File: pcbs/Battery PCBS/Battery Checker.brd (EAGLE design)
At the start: 49.5 x 49.5 mm, 26 parts, among them Q1 BSS138, Q2 BSS138

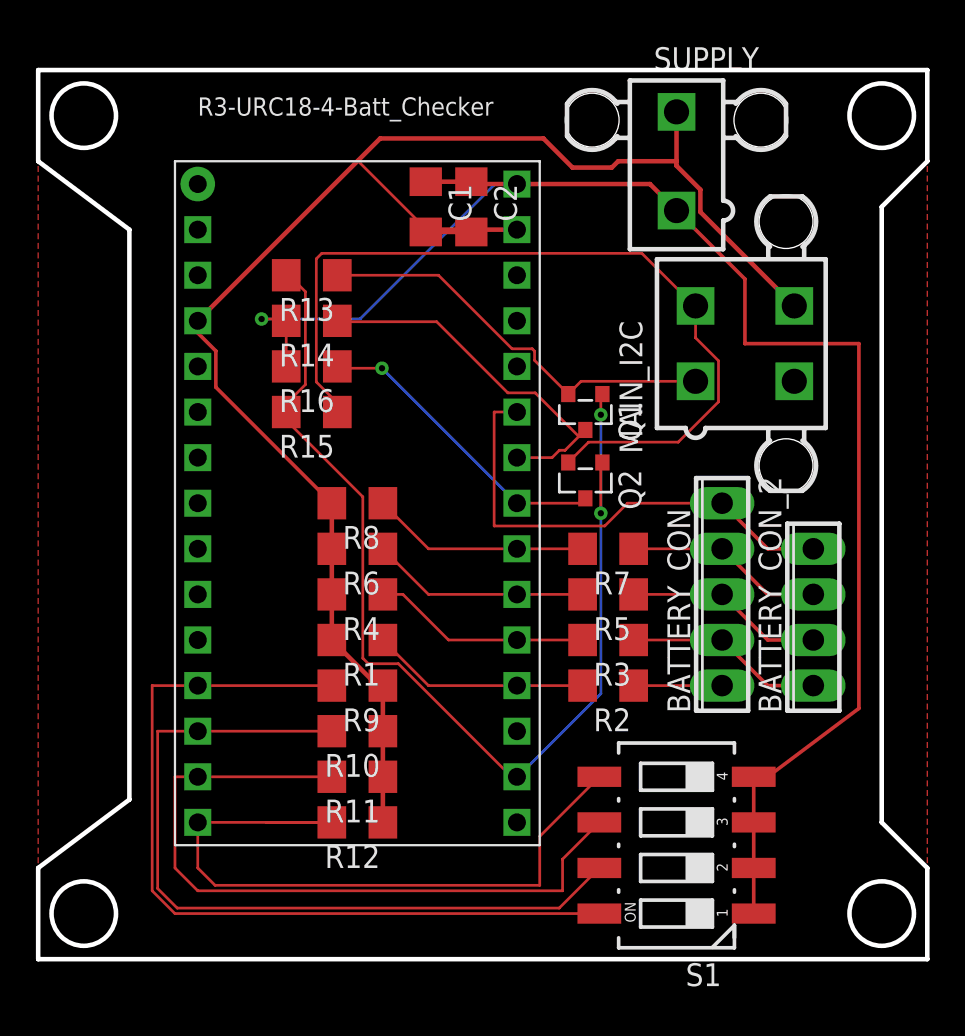
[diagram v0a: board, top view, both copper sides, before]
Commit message: Final commit for battery pcb, added resistor values #2
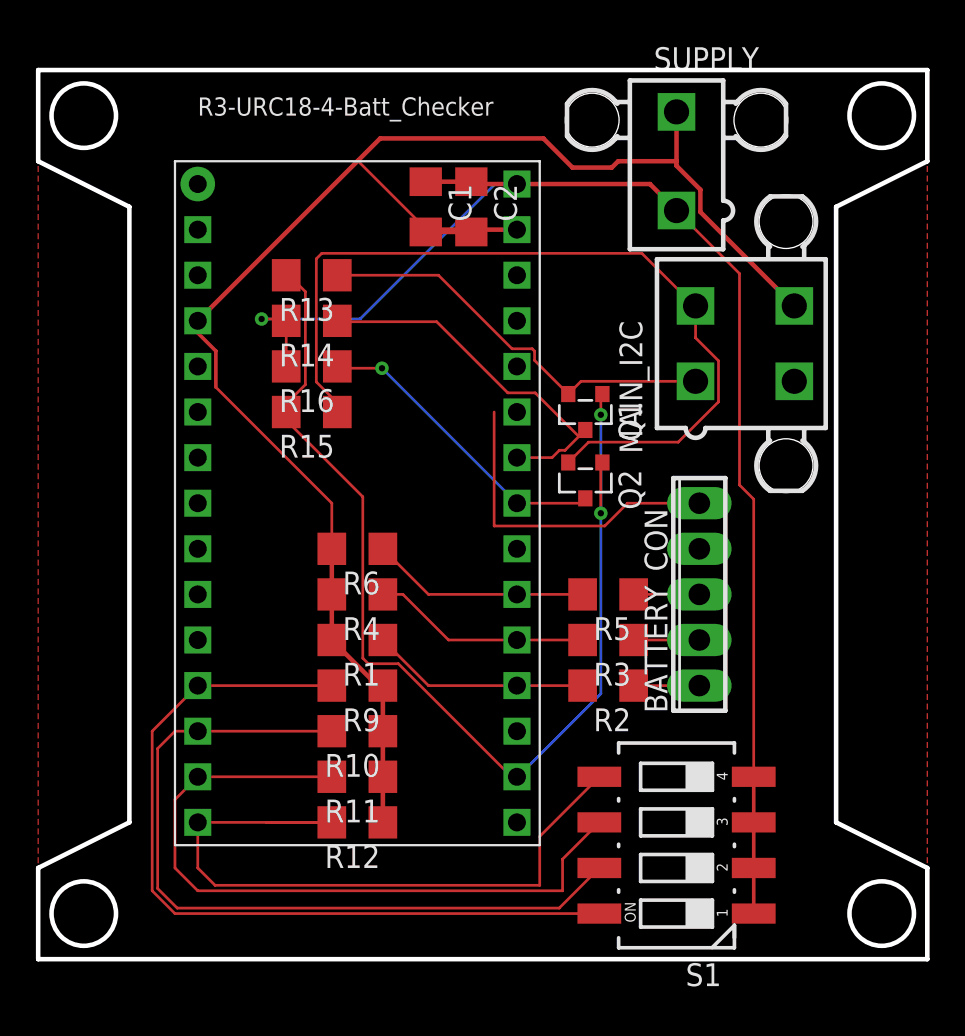
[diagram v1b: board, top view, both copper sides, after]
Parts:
- removed BATTERY_CON_2: (no value), con-phoenix-254:4POL254
- removed R7, R8: (no value), rcl:R1206
- R1, R4, R5, R6: value (none) -> 10k
- R2: value (none) -> 30k
- R3: value (none) -> 20k
- moved BATTERY_CON 1.27 mm to (57.1, 66.0)
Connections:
- removed net N$4: R7.2, R8.1, U$1.A3
- net BATT2: no longer BATTERY_CON_2.1
- net BATT3: no longer BATTERY_CON_2.2
- net BATT4: now also U$1.A3; no longer BATTERY_CON_2.3, R7.1
- net BATT5: no longer BATTERY_CON_2.4, U$1.A6
- net GND: now also MAIN_I2C.3; no longer R8.2
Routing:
- net N$4: track 12.2 -> 0.00 mm
- net BATT4: track 11.1 -> 0.00 mm
- net VIN: track 85.6 -> 77.0 mm
- net BATT5: track 27.0 -> 18.3 mm
- net BATT3: track 11.1 -> 3.66 mm
- net BATT2: track 11.1 -> 3.66 mm
- net ADD1: track 46.9 -> 45.4 mm
- net BATT1: track 4.93 -> 3.66 mm
- net ADD3: track 40.7 -> 40.0 mm
- net ADD2: track 44.6 -> 44.0 mm
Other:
- outline, holes or cut-outs redrawn

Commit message: Final final changes
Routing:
- net BATT5: track 18.3 -> 0.00 mm
- net BATT4: track 0.00 -> 10.2 mm
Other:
- outline, holes or cut-outs redrawn
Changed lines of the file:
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@@
 <setting verticaltext="up"/>
 </settings>
-<grid distance="50" unitdist="mil" unit="inch" style="lines" multiple="1" display="yes" altdistance="5" altunitdist="mil" altunit="inch"/>
+<grid distance="50" unitdist="mil" unit="mm" style="lines" multiple="1" display="yes" altdistance="5" altunitdist="mil" altunit="mm"/>
 <layers>
 <layer number="1" name="Top" color="4" fill="1" visible="yes" active="yes"/>
@@
 <board>
 <plain>
-<circle x="22.86" y="92.71" radius="1.79605" width="0.254" layer="20"/>
-<circle x="22.86" y="48.26" radius="1.79605" width="0.254" layer="20"/>
-<circle x="67.31" y="92.71" radius="1.79605" width="0.254" layer="20"/>
-<circle x="67.31" y="48.26" radius="1.79605" width="0.254" layer="20"/>
 <wire x1="20.32" y1="95.25" x2="20.32" y2="90.17" width="0.254" layer="20"/>
 <wire x1="20.32" y1="90.17" x2="25.4" y2="87.63" width="0.254" layer="20"/>
@@
 <wire x1="69.85" y1="95.25" x2="20.32" y2="95.25" width="0.254" layer="20"/>
 <text x="29.21" y="92.71" size="1.016" layer="21">R3-URC18-4-Batt_Checker</text>
+<dimension x1="20.32" y1="95.25" x2="69.85" y2="95.25" x3="45.085" y3="97.79" textsize="1.778" layer="20" unit="mil" visible="yes"/>
+<dimension x1="20.32" y1="95.25" x2="20.32" y2="45.72" x3="13.97" y3="70.485" textsize="1.778" layer="20" unit="mil" visible="yes"/>
+<dimension x1="20.32" y1="95.25" x2="25.4" y2="87.63" x3="8.89" y3="91.44" textsize="1.778" layer="20" dtype="vertical" unit="mil" visible="yes"/>
+<dimension x1="20.32" y1="95.25" x2="25.4" y2="87.63" x3="22.86" y3="101.6" textsize="1.778" layer="20" dtype="horizontal" unit="mil" visible="yes"/>
+<hole x="22.86" y="92.71" drill="3.25"/>
+<hole x="67.31" y="92.71" drill="3.25"/>
+<hole x="67.31" y="48.26" drill="3.25"/>
+<hole x="22.86" y="48.26" drill="3.25"/>
 </plain>
 <attributes>
@@
 <contactref element="BATTERY_CON" pad="4"/>
 <contactref element="U$1" pad="A3"/>
-<wire x1="46.99" y1="68.58" x2="57.15" y2="68.58" width="0" layer="19" extent="1-1"/>
+<wire x1="57.15" y1="68.58" x2="46.99" y2="68.58" width="0.1524" layer="1"/>
 </signal>
 <signal name="BATT5">
 <contactref element="BATTERY_CON" pad="5"/>
-<wire x1="57.15" y1="71.12" x2="53.15105625" y2="71.12" width="0.1524" layer="1"/>
-<wire x1="45.72" y1="69.85" x2="45.72" y2="76.2" width="0.1524" layer="1"/>
-<wire x1="51.88105625" y1="69.85" x2="45.72" y2="69.85" width="0.1524" layer="1"/>
-<wire x1="53.15105625" y1="71.12" x2="51.88105625" y2="69.85" width="0.1524" layer="1"/>
 </signal>
 <signal name="SDA">
